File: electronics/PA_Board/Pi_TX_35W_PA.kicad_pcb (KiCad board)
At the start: 4 copper layers, 100 x 100 mm, 160 parts, among them J1 USB_B_Micro, J2 Conn_01x05, J3 Conn_01x05, J4 Conn_01x04, J5 Conn_01x02, J6 Conn_Coaxial, J7 Conn_Coaxial, J8 Conn_Coaxial, J9 Conn_Coaxial, K1 G6E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

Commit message: PCB updates and gerbers
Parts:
- removed Directional Coupler: Wiggly Coupler, Pi_Tx:Wiggly Coupler
- added LOGO1: Logo_Open_Hardware_Small, Symbol:OSHW-Logo2_9.8x8mm_SilkScreen, F.Cu at (149.3, 112.0)
- added U11: Directional_Coupler, Pi_Tx:Wiggly Coupler, F.Cu at (165.2, 116.6)
- D2: footprint LED_SMD:LED-APA102-2020 -> Pi_Tx:LED-APA102-2020
- H1, H2, H3, H4: value MountingHole -> MountingHole_Pad; footprint MountingHole:MountingHole_4.3mm_M4 -> MountingHole:MountingHole_4.3mm_M4_DIN965_Pad
- L2: footprint Inductor_SMD:L_7.3x7.3_H3.5 -> Inductor_SMD:L_7.3x7.3_H4.5
- L5, L7: footprint Inductor_SMD:L_Neosid_Air-Coil_SML_3turn_HDM0331A -> Pi_Tx:Wire_Inductor 12x8.5
- L6: footprint Inductor_SMD:L_Neosid_Air-Coil_SML_3turn_HDM0331A -> Pi_Tx:Wire_Inductor 15.5x8.5
- U2, U3: footprint Package_SO:SO-8_3.9x4.9mm_P1.27mm -> Package_SO:SOIC-8_3.9x4.9mm_P1.27mm
- U4: footprint Package_SO:SOIC-8-1EP_3.9x4.9mm_P1.27mm_EP2.41x3.3mm_ThermalVias -> Package_SO:SOIC-8-1EP_3.9x4.9mm_P1.27mm_EP2.41x3.3mm
- moved C13 62.1 mm to (133.7, 116.1), turned to 180 degrees
- moved D9 20.1 mm to (131.1, 120.5)
- moved R30 18.8 mm to (128.2, 105.6), turned to -90 degrees
- moved R31 15.3 mm to (128.8, 109.0)
- moved R45 15.0 mm to (167.8, 123.5), turned to -90 degrees
- moved Q1 12.8 mm to (193.5, 79.1), turned to 0 degrees
- moved L5 12.7 mm to (181.1, 82.1), turned to -90 degrees
- moved R41 12.3 mm to (165.8, 109.8), turned to -90 degrees
- moved C14 11.5 mm to (137.2, 115.8), turned to 180 degrees
- moved C39 9.19 mm to (182.1, 93.5)
- moved C43 8.56 mm to (154.1, 87.2)
- moved C41 7.76 mm to (166.8, 87.3)
- moved L6 7.26 mm to (170.5, 93.4), turned to 180 degrees
- moved C17 5.53 mm to (145.4, 104.4)
- moved C18 5.53 mm to (147.4, 104.4)
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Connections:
- net /PA_Power/VDD_GAIN renamed +5V
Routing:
- net GND: track 76.6 -> 334.4 mm, vias 8 -> 362
- net +12V: track 0.00 -> 176.1 mm, vias 0 -> 19
- net /PA_Power/Int_SDA: track 0.00 -> 106.2 mm, vias 0 -> 6
- net /PA_Power/Int_SCL: track 0.00 -> 97.3 mm, vias 0 -> 6
- net /PA_Protection/VFwd: track 0.00 -> 75.8 mm, vias 0 -> 2
- net Net-(C21-Pad1): track 0.00 -> 68.2 mm, vias 0 -> 5
- net +5V: track 0.00 -> 67.5 mm, vias 0 -> 2
- net /PA_Protection/Temp_INT: track 0.00 -> 66.5 mm, vias 0 -> 2
- net /PA_Protection/TX_Relay: track 0.00 -> 56.0 mm, vias 0 -> 2
- net /PA_Protection/Slave_SDA: track 0.00 -> 48.2 mm, vias 0 -> 2
- net /PA_Protection/Slave_INT: track 0.00 -> 47.0 mm, vias 0 -> 2
- net /PA_Power/En_Vgg_PA: track 0.00 -> 43.2 mm, vias 0 -> 2
- net /PA_Protection/ADC_Vgg_PA: track 0.00 -> 42.6 mm, vias 0 -> 2
- net /PA_Power/VDD_PA: track 0.00 -> 39.4 mm, vias 0 -> 4
- net /PA_Protection/Slave_SCL: track 0.00 -> 36.7 mm
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- added copper zone on B.Cu, net +12V
- added copper zone on F.Cu, net +12V
- added copper zone on In1.Cu, net +12V
- added copper zone on In2.Cu, net +12V
- added copper zone on In2.Cu, net +3.3V
- added copper zone on F.Cu, net /PA_Power/VDD_PA
- added copper zone on In2.Cu, net /PA_Power/VDD_PA
- added copper zone on B.Cu, net GND
- added copper zone on F.Cu, net GND
- added copper zone on In2.Cu, net GND
- added copper zone on F.Cu, net Net-(C31-Pad1)
- added copper zone on In2.Cu, net Net-(C31-Pad1)
- added copper zone on B.Cu, net Net-(J5-Pad1)
- added copper zone on F.Cu, net Net-(J5-Pad1)
- added copper zone on In1.Cu, net Net-(J5-Pad1)
- added copper zone on In2.Cu, net Net-(J5-Pad1)
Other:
- outline, holes or cut-outs redrawn
- board text added: "RADARC 2m 30W PA for pi-transceiver"
- board text added: "Tx Monitor"
- board text added: "V1.0"
- board text added: "www.radarc.org Nov. 2022"
- board text removed: "TX Monitor"

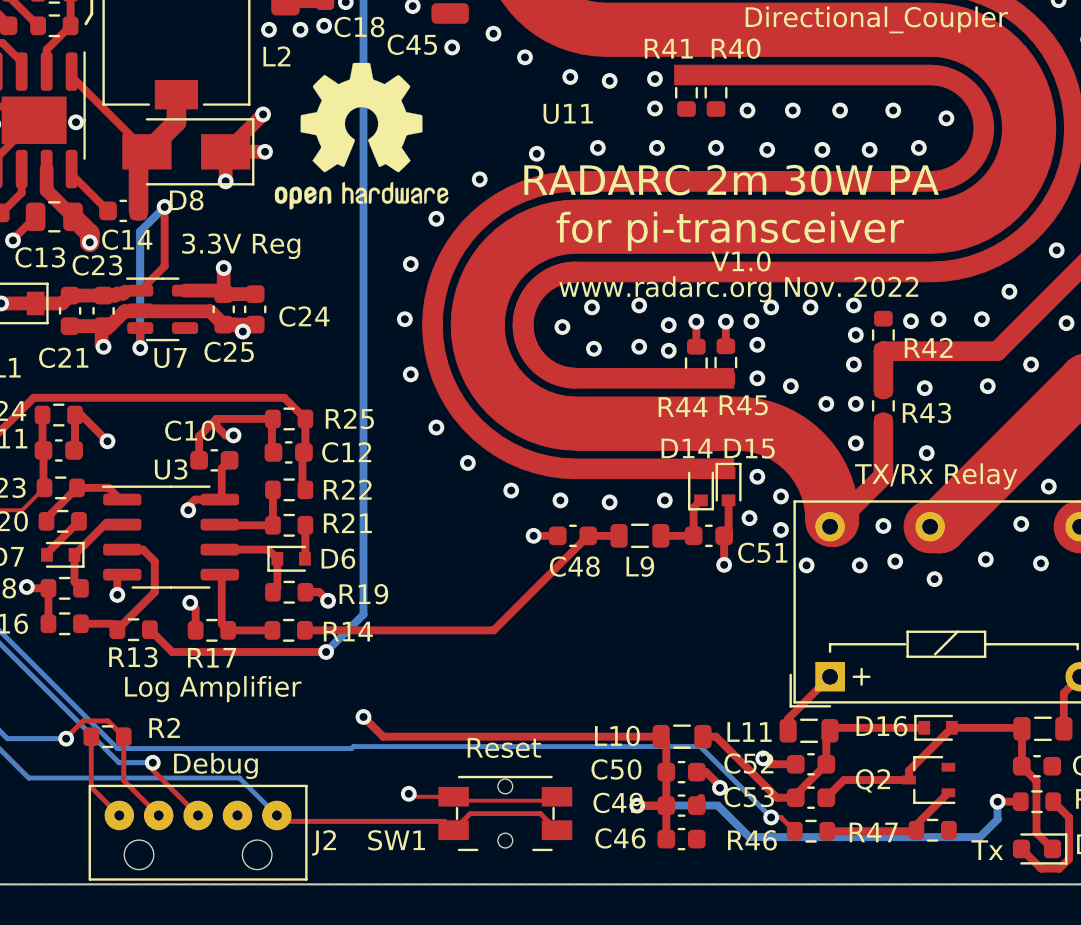
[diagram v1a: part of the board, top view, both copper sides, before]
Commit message: Update Kicad Schematic and PCB
Fixed: D8 was reversed, Q2 wrong footprint.
Some component values added or changed
Documentation added
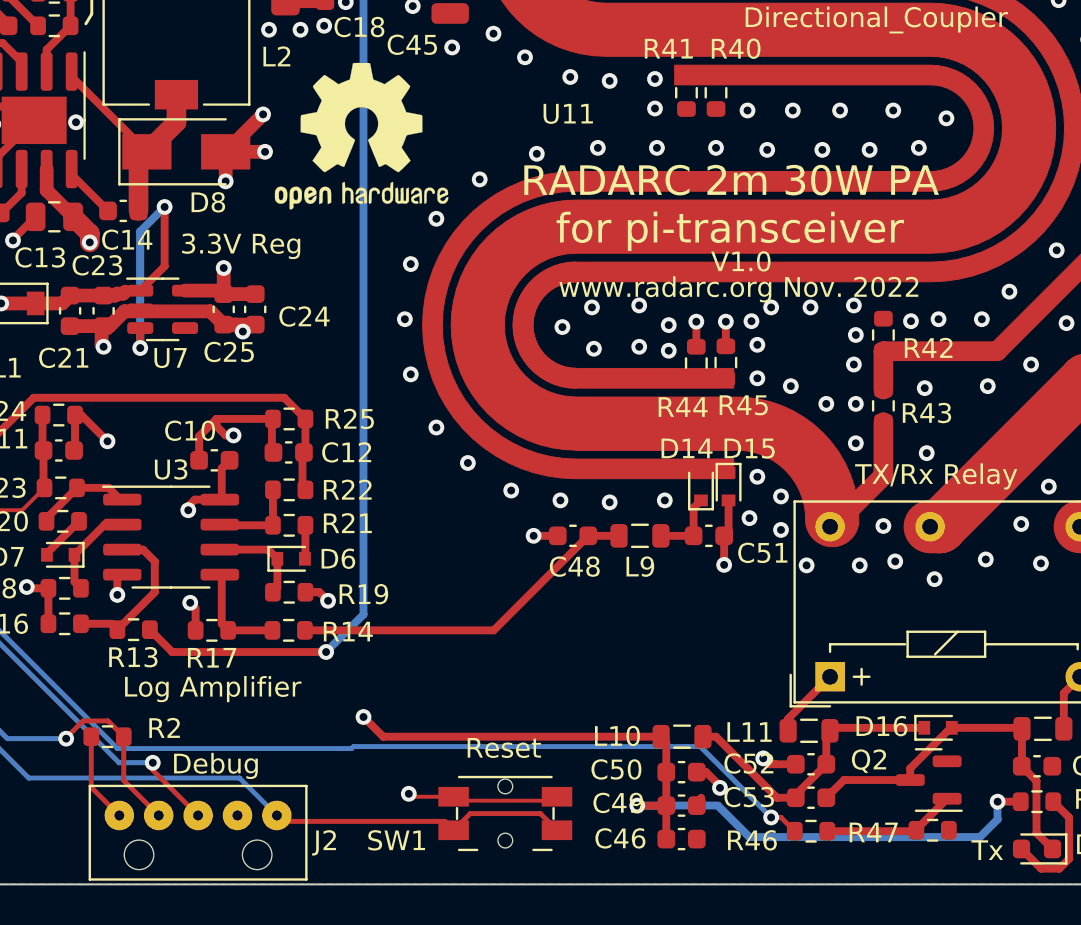
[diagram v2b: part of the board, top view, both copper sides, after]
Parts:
- C38: value C -> 9p1
- C39, C42: value C -> 18p
- C40, C43: value C -> NF
- C41: value C -> 3p
- C45: value C -> 6p8
- L5, L7: value L -> 34nH
- L6: value L -> 46nH
- Q2: footprint Package_TO_SOT_SMD:SOT-323_SC-70 -> Package_TO_SOT_SMD:SOT-23
- R12: value 10k -> 47k
- R15: value 100k -> 10k
- R33: value 1k -> 470
- R34: value 470 -> 1k
- R36: value 4m -> 10m
- turned D8 to 0 degrees
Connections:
- D8 pad 1: GND -> Net-(C14-Pad1)
- D8 pad 2: Net-(C14-Pad1) -> GND

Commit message: Add PA Board tests
Add PA Board Arduino Tests
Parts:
- Q1: value SUD09P10-195 -> RD3G01BAT
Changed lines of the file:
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@@
       (effects (font (size 1 1) (thickness 0.15)))
     )
-    (fp_text value "SUD09P10-195" (at 0 4.5) (layer "F.Fab")
+    (fp_text value "RD3G01BAT" (at 0 4.5) (layer "F.Fab")
       (effects (font (size 1 1) (thickness 0.15)))
     )

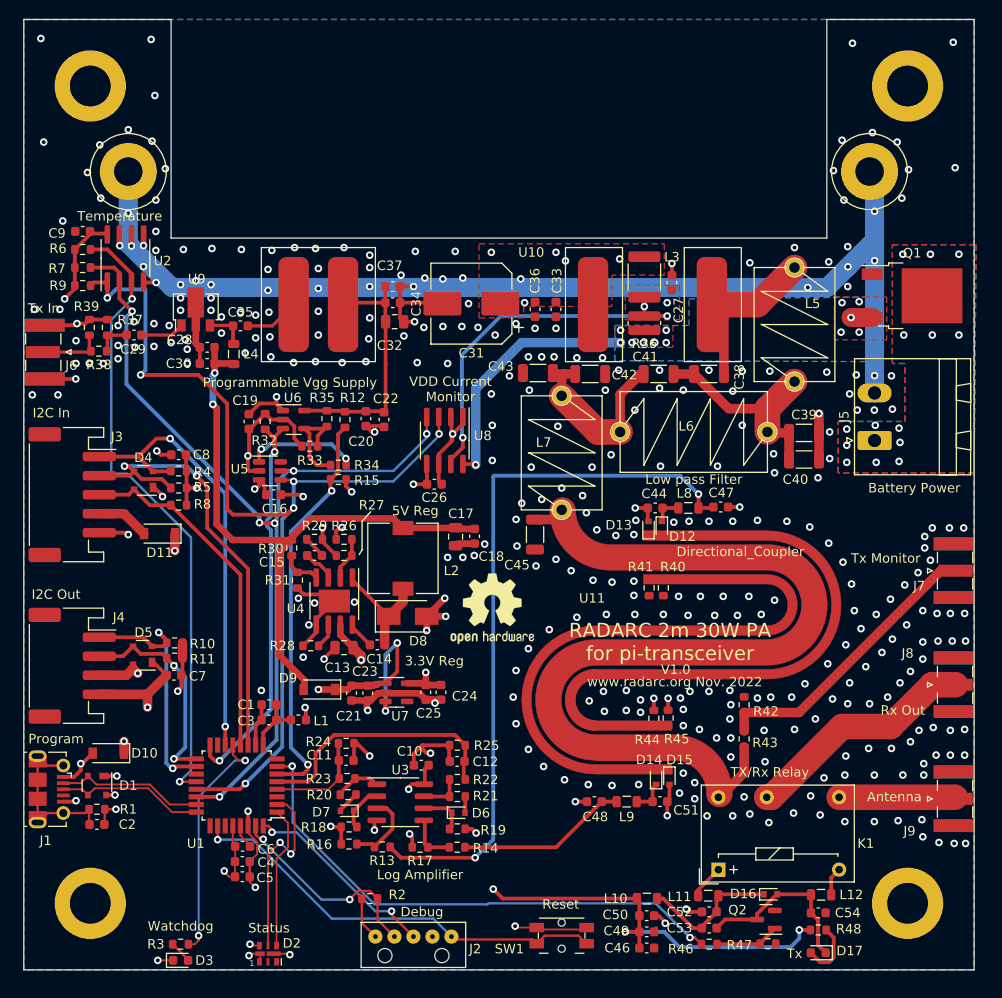
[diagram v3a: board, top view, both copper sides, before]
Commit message: Merge branch 'main' of https://github.com/M0LTE/pi-transceiver
Addition of PA Board version 2 Kicad files
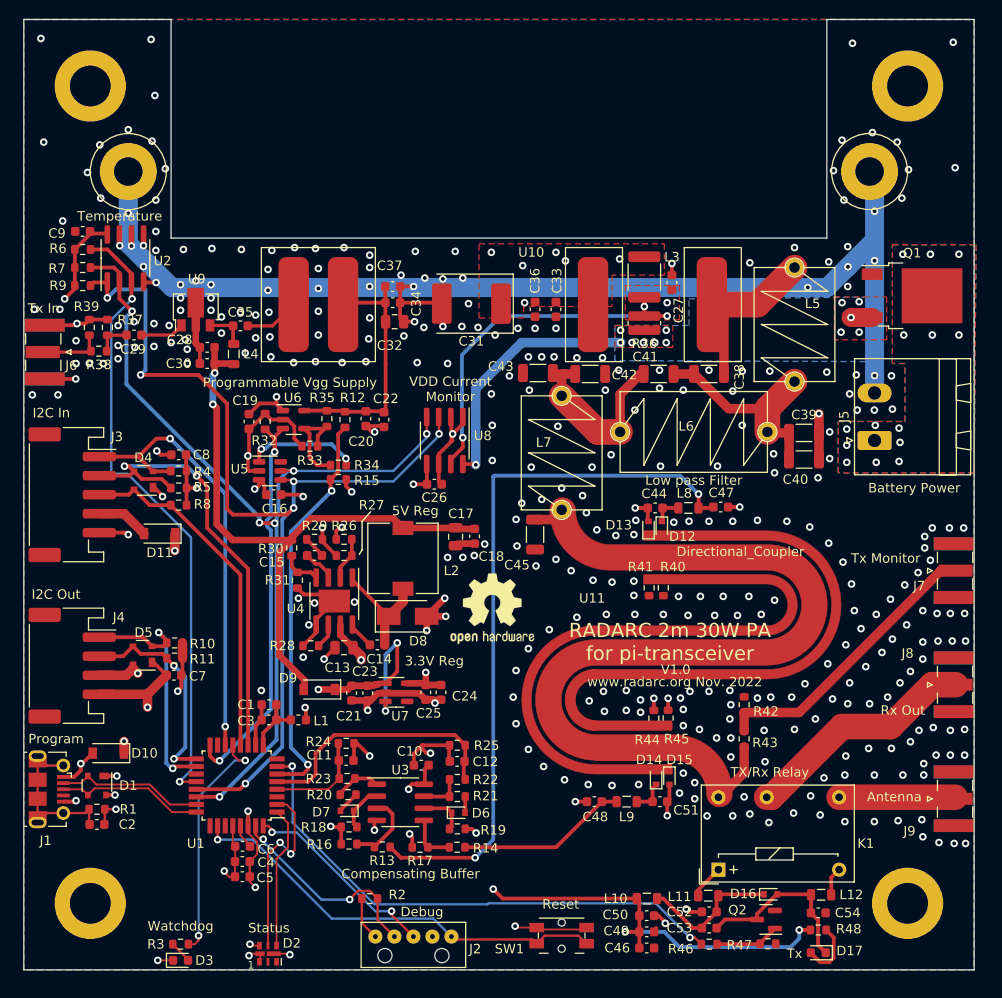
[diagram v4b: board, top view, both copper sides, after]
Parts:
- C31: footprint Capacitor_SMD:CP_Elec_8x6.7 -> Capacitor_Tantalum_SMD:CP_EIA-7360-38_Kemet-E
- D17: value LED -> LED_Red
- D3: value LED -> LED_Orange
- R22, R23: value 330 -> 330R
- R33: value 470 -> 470R
- R37, R39, R40, R41, R44, R45: value 150 -> 150R
- R38: value 37.4 -> 37.4R
- R42: value 49.9 -> 49.9R
- U5: value MCP4725xxx-xCH -> MCP4725
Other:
- board text added: "Compensating Buffer"
- board text removed: "Log Amplifier"
